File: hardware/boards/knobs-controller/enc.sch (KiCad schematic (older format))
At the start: 11 parts, among them SW2 Rotary Encoder

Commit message: minor cleanup
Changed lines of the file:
@@
 $Descr A4 11693 8268
 encoding utf-8
-Sheet 5 6
+Sheet 3 6
 Title ""
 Date ""
@@
 AR Path="/5D86641C/5D8716A9/5D98B23E" Ref="SW3"  Part="1"
 AR Path="/5D86641C/5D87B0CB/5D98B23E" Ref="SW?"  Part="1"
-F 0 "SW3" H 5500 4570 70  0000 L BNN
+F 0 "SW2" H 5500 4570 70  0000 L BNN
 F 1 "Rotary Encoder" H 5500 3655 70  0000 L BNN
 F 2 "knobs:ENCODER_LED_3_KIT" H 6000 4150 50  0001 C CNN
@@
 AR Path="/5D86641C/5D8716A9/5D98B244" Ref="R28"  Part="1"
 AR Path="/5D86641C/5D87B0CB/5D98B244" Ref="R?"  Part="1"
-F 0 "R28" H 6850 5059 59  0000 L BNN
+F 0 "R19" H 6850 5059 59  0000 L BNN
 F 1 "10k" H 6850 4870 59  0000 L BNN
 F 2 "knobs:R0805" H 7000 5000 50  0001 C CNN
@@
 AR Path="/5D86641C/5D8716A9/5D98B24A" Ref="R25"  Part="1"
 AR Path="/5D86641C/5D87B0CB/5D98B24A" Ref="R?"  Part="1"
-F 0 "R25" H 4050 3709 59  0000 L BNN
+F 0 "R12" H 4050 3709 59  0000 L BNN
 F 1 "10k" H 4050 3520 59  0000 L BNN
 F 2 "knobs:R0805" H 4200 3650 50  0001 C CNN
@@
 AR Path="/5D86641C/5D8716A9/5D98B250" Ref="R24"  Part="1"
 AR Path="/5D86641C/5D87B0CB/5D98B250" Ref="R?"  Part="1"
-F 0 "R24" H 3750 4009 59  0000 L BNN
+F 0 "R11" H 3750 4009 59  0000 L BNN
 F 1 "10k" H 3750 3820 59  0000 L BNN
 F 2 "knobs:R0805" H 3900 3950 50  0001 C CNN
@@
 AR Path="/5D86641C/5D8716A9/5D98B256" Ref="R27"  Part="1"
 AR Path="/5D86641C/5D87B0CB/5D98B256" Ref="R?"  Part="1"
-F 0 "R27" H 5050 3709 59  0000 L BNN
+F 0 "R17" H 5050 3709 59  0000 L BNN
 F 1 "10k" H 5050 3520 59  0000 L BNN
 F 2 "knobs:R0805" H 5200 3650 50  0001 C CNN
@@
 AR Path="/5D86641C/5D8716A9/5D98B25C" Ref="R26"  Part="1"
 AR Path="/5D86641C/5D87B0CB/5D98B25C" Ref="R?"  Part="1"
-F 0 "R26" H 4750 4409 59  0000 L BNN
+F 0 "R14" H 4750 4409 59  0000 L BNN
 F 1 "10k" H 4750 4220 59  0000 L BNN
 F 2 "knobs:R0805" H 4900 4350 50  0001 C CNN
@@
 AR Path="/5D86641C/5D8716A9/5D98B262" Ref="C14"  Part="1"
 AR Path="/5D86641C/5D87B0CB/5D98B262" Ref="C?"  Part="1"
-F 0 "C14" H 4660 4765 59  0000 L BNN
+F 0 "C12" H 4660 4765 59  0000 L BNN
 F 1 "10nF" H 4660 4465 59  0001 L BNN
 F 2 "knobs:C0805" H 4600 4650 50  0001 C CNN
@@
 AR Path="/5D86641C/5D8716A9/5D98B268" Ref="C13"  Part="1"
 AR Path="/5D86641C/5D87B0CB/5D98B268" Ref="C?"  Part="1"
-F 0 "C13" H 3660 4265 59  0000 L BNN
+F 0 "C3" H 3660 4265 59  0000 L BNN
 F 1 "10nF" H 3660 4065 59  0000 L BNN
 F 2 "knobs:C0805" H 3600 4250 50  0001 C CNN
@@
 AR Path="/5D86641C/5D8716A9/5D98B26E" Ref="R29"  Part="1"
 AR Path="/5D86641C/5D87B0CB/5D98B26E" Ref="R?"  Part="1"
-F 0 "R29" H 7050 3909 59  0000 L BNN
+F 0 "R21" H 7050 3909 59  0000 L BNN
 F 1 "10" H 7050 3720 59  0000 L BNN
 F 2 "knobs:R0805" H 7200 3850 50  0001 C CNN
@@
 AR Path="/5D86641C/5D8716A9/5D98B274" Ref="R30"  Part="1"
 AR Path="/5D86641C/5D87B0CB/5D98B274" Ref="R?"  Part="1"
-F 0 "R30" H 7050 4209 59  0000 L BNN
+F 0 "R22" H 7050 4209 59  0000 L BNN
 F 1 "10" H 7050 4020 59  0000 L BNN
 F 2 "knobs:R0805" H 7200 4150 50  0001 C CNN
@@
 AR Path="/5D86641C/5D8716A9/5D98B27A" Ref="R31"  Part="1"
 AR Path="/5D86641C/5D87B0CB/5D98B27A" Ref="R?"  Part="1"
-F 0 "R31" H 7050 4509 59  0000 L BNN
+F 0 "R23" H 7050 4509 59  0000 L BNN
 F 1 "10" H 7050 4320 59  0000 L BNN
 F 2 "knobs:R0805" H 7200 4450 50  0001 C CNN
@@
 AR Path="/5D86641C/5D8716A9/5D98B281" Ref="#+3V020"  Part="1"
 AR Path="/5D86641C/5D87B0CB/5D98B281" Ref="#+3V?"  Part="1"
-F 0 "#+3V020" H 5200 3250 50  0001 C CNN
+F 0 "#+3V017" H 5200 3250 50  0001 C CNN
 F 1 "+3V3" H 5200 3372 59  0000 C CNN
 F 2 "" H 5200 3250 50  0001 C CNN
@@
 AR Path="/5D86641C/5D8716A9/5D98B287" Ref="#GND030"  Part="1"
 AR Path="/5D86641C/5D87B0CB/5D98B287" Ref="#GND?"  Part="1"
-F 0 "#GND030" H 4600 4950 50  0001 C CNN
+F 0 "#GND026" H 4600 4950 50  0001 C CNN
 F 1 "GND" H 4600 4829 59  0000 C CNN
 F 2 "" H 4600 4950 50  0001 C CNN
@@
 AR Path="/5D86641C/5D8716A9/5D98B28D" Ref="#+3V019"  Part="1"
 AR Path="/5D86641C/5D87B0CB/5D98B28D" Ref="#+3V?"  Part="1"
-F 0 "#+3V019" H 4200 3250 50  0001 C CNN
+F 0 "#+3V016" H 4200 3250 50  0001 C CNN
 F 1 "+3V3" H 4200 3372 59  0000 C CNN
 F 2 "" H 4200 3250 50  0001 C CNN
@@
 AR Path="/5D86641C/5D8716A9/5D98B293" Ref="#+3V021"  Part="1"
 AR Path="/5D86641C/5D87B0CB/5D98B293" Ref="#+3V?"  Part="1"
-F 0 "#+3V021" H 6700 3650 50  0001 C CNN
+F 0 "#+3V018" H 6700 3650 50  0001 C CNN
 F 1 "+3V3" H 6700 3772 59  0000 C CNN
 F 2 "" H 6700 3650 50  0001 C CNN
@@
 AR Path="/5D86641C/5D8716A9/5D98B299" Ref="#GND029"  Part="1"
 AR Path="/5D86641C/5D87B0CB/5D98B299" Ref="#GND?"  Part="1"
-F 0 "#GND029" H 3600 4550 50  0001 C CNN
+F 0 "#GND025" H 3600 4550 50  0001 C CNN
 F 1 "GND" H 3600 4429 59  0000 C CNN
 F 2 "" H 3600 4550 50  0001 C CNN
@@
 AR Path="/5D86641C/5D8716A9/5D98B29F" Ref="#GND032"  Part="1"
 AR Path="/5D86641C/5D87B0CB/5D98B29F" Ref="#GND?"  Part="1"
-F 0 "#GND032" H 7000 5300 50  0001 C CNN
+F 0 "#GND028" H 7000 5300 50  0001 C CNN
 F 1 "GND" H 7000 5179 59  0000 C CNN
 F 2 "" H 7000 5300 50  0001 C CNN
@@
 AR Path="/5D86641C/5D8716A9/5D98B2A5" Ref="#GND031"  Part="1"
 AR Path="/5D86641C/5D87B0CB/5D98B2A5" Ref="#GND?"  Part="1"
-F 0 "#GND031" H 5300 4550 50  0001 C CNN
+F 0 "#GND027" H 5300 4550 50  0001 C CNN
 F 1 "GND" H 5300 4429 59  0000 C CNN
 F 2 "" H 5300 4550 50  0001 C CNN

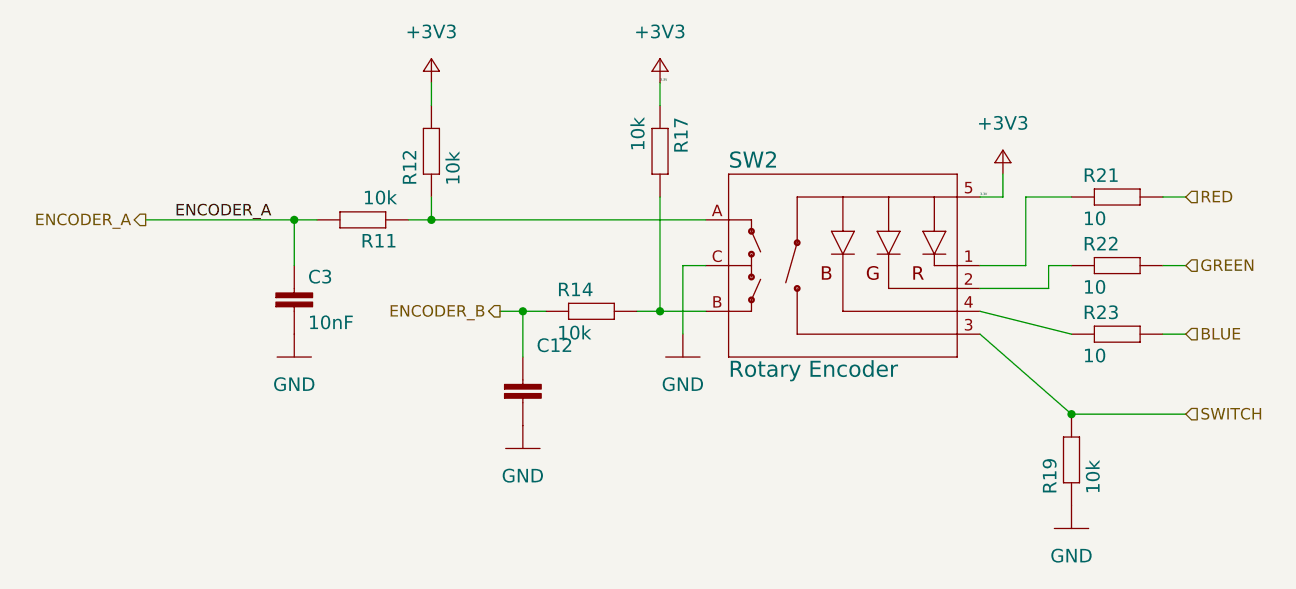
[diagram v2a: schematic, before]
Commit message: correction: tx, rx connected
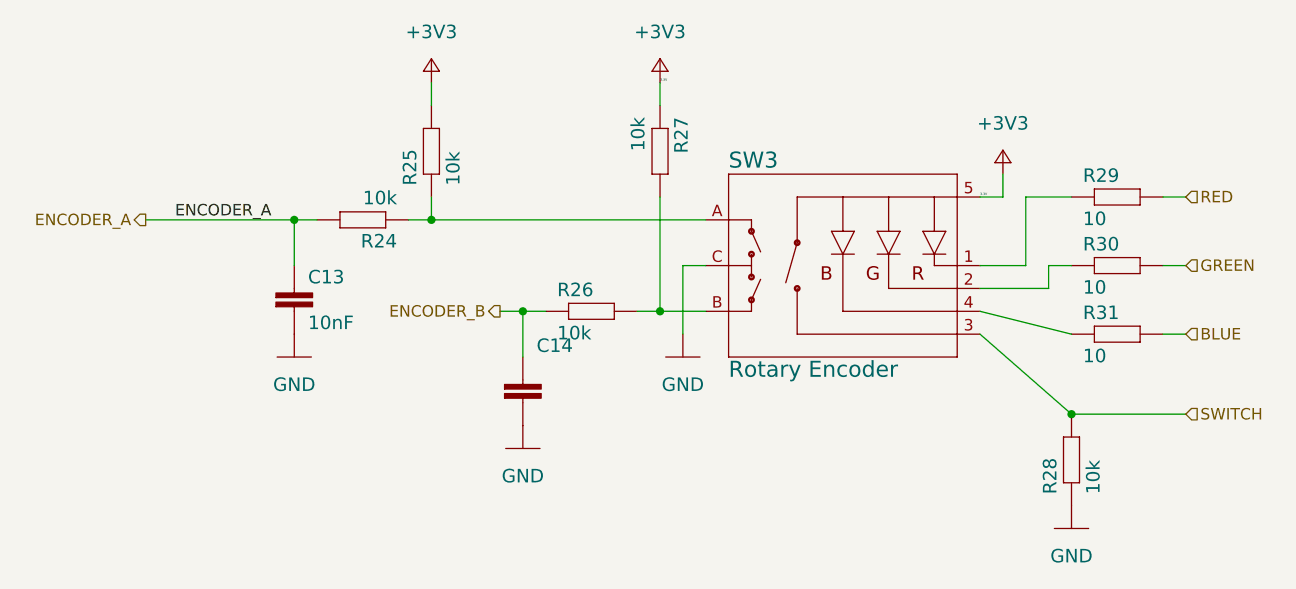
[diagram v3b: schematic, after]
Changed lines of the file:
@@
-EESchema Schematic File Version 4
-LIBS:knobs-cache
+EESchema Schematic File Version 5
 EELAYER 30 0
 EELAYER END
@@
 Comment3 ""
 Comment4 ""
+Comment5 ""
+Comment6 ""
+Comment7 ""
+Comment8 ""
+Comment9 ""
 $EndDescr
 Wire Wire Line
@@
 AR Path="/5D86641C/5D8716A9/5D98B23E" Ref="SW3"  Part="1"
 AR Path="/5D86641C/5D87B0CB/5D98B23E" Ref="SW?"  Part="1"
-F 0 "SW2" H 5500 4570 70  0000 L BNN
+F 0 "SW3" H 5500 4570 70  0000 L BNN
 F 1 "Rotary Encoder" H 5500 3655 70  0000 L BNN
 F 2 "knobs:ENCODER_LED_3_KIT" H 6000 4150 50  0001 C CNN
@@
 AR Path="/5D86641C/5D8716A9/5D98B244" Ref="R28"  Part="1"
 AR Path="/5D86641C/5D87B0CB/5D98B244" Ref="R?"  Part="1"
-F 0 "R19" H 6850 5059 59  0000 L BNN
+F 0 "R28" H 6850 5059 59  0000 L BNN
 F 1 "10k" H 6850 4870 59  0000 L BNN
 F 2 "knobs:R0805" H 7000 5000 50  0001 C CNN
@@
 AR Path="/5D86641C/5D8716A9/5D98B24A" Ref="R25"  Part="1"
 AR Path="/5D86641C/5D87B0CB/5D98B24A" Ref="R?"  Part="1"
-F 0 "R12" H 4050 3709 59  0000 L BNN
+F 0 "R25" H 4050 3709 59  0000 L BNN
 F 1 "10k" H 4050 3520 59  0000 L BNN
 F 2 "knobs:R0805" H 4200 3650 50  0001 C CNN
@@
 AR Path="/5D86641C/5D8716A9/5D98B250" Ref="R24"  Part="1"
 AR Path="/5D86641C/5D87B0CB/5D98B250" Ref="R?"  Part="1"
-F 0 "R11" H 3750 4009 59  0000 L BNN
+F 0 "R24" H 3750 4009 59  0000 L BNN
 F 1 "10k" H 3750 3820 59  0000 L BNN
 F 2 "knobs:R0805" H 3900 3950 50  0001 C CNN
@@
 AR Path="/5D86641C/5D8716A9/5D98B256" Ref="R27"  Part="1"
 AR Path="/5D86641C/5D87B0CB/5D98B256" Ref="R?"  Part="1"
-F 0 "R17" H 5050 3709 59  0000 L BNN
+F 0 "R27" H 5050 3709 59  0000 L BNN
 F 1 "10k" H 5050 3520 59  0000 L BNN
 F 2 "knobs:R0805" H 5200 3650 50  0001 C CNN
@@
 AR Path="/5D86641C/5D8716A9/5D98B25C" Ref="R26"  Part="1"
 AR Path="/5D86641C/5D87B0CB/5D98B25C" Ref="R?"  Part="1"
-F 0 "R14" H 4750 4409 59  0000 L BNN
+F 0 "R26" H 4750 4409 59  0000 L BNN
 F 1 "10k" H 4750 4220 59  0000 L BNN
 F 2 "knobs:R0805" H 4900 4350 50  0001 C CNN
@@
 AR Path="/5D86641C/5D8716A9/5D98B262" Ref="C14"  Part="1"
 AR Path="/5D86641C/5D87B0CB/5D98B262" Ref="C?"  Part="1"
-F 0 "C12" H 4660 4765 59  0000 L BNN
+F 0 "C14" H 4660 4765 59  0000 L BNN
 F 1 "10nF" H 4660 4465 59  0001 L BNN
 F 2 "knobs:C0805" H 4600 4650 50  0001 C CNN
@@
 AR Path="/5D86641C/5D8716A9/5D98B268" Ref="C13"  Part="1"
 AR Path="/5D86641C/5D87B0CB/5D98B268" Ref="C?"  Part="1"
-F 0 "C3" H 3660 4265 59  0000 L BNN
+F 0 "C13" H 3660 4265 59  0000 L BNN
 F 1 "10nF" H 3660 4065 59  0000 L BNN
 F 2 "knobs:C0805" H 3600 4250 50  0001 C CNN
@@
 AR Path="/5D86641C/5D8716A9/5D98B26E" Ref="R29"  Part="1"
 AR Path="/5D86641C/5D87B0CB/5D98B26E" Ref="R?"  Part="1"
-F 0 "R21" H 7050 3909 59  0000 L BNN
+F 0 "R29" H 7050 3909 59  0000 L BNN
 F 1 "10" H 7050 3720 59  0000 L BNN
 F 2 "knobs:R0805" H 7200 3850 50  0001 C CNN
@@
 AR Path="/5D86641C/5D8716A9/5D98B274" Ref="R30"  Part="1"
 AR Path="/5D86641C/5D87B0CB/5D98B274" Ref="R?"  Part="1"
-F 0 "R22" H 7050 4209 59  0000 L BNN
+F 0 "R30" H 7050 4209 59  0000 L BNN
 F 1 "10" H 7050 4020 59  0000 L BNN
 F 2 "knobs:R0805" H 7200 4150 50  0001 C CNN
@@
 AR Path="/5D86641C/5D8716A9/5D98B27A" Ref="R31"  Part="1"
 AR Path="/5D86641C/5D87B0CB/5D98B27A" Ref="R?"  Part="1"
-F 0 "R23" H 7050 4509 59  0000 L BNN
+F 0 "R31" H 7050 4509 59  0000 L BNN
 F 1 "10" H 7050 4320 59  0000 L BNN
 F 2 "knobs:R0805" H 7200 4450 50  0001 C CNN

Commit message: v1.7: merge knobs and top breakout in to single board, remove fpc connector, replace with standard 0.1' pin header
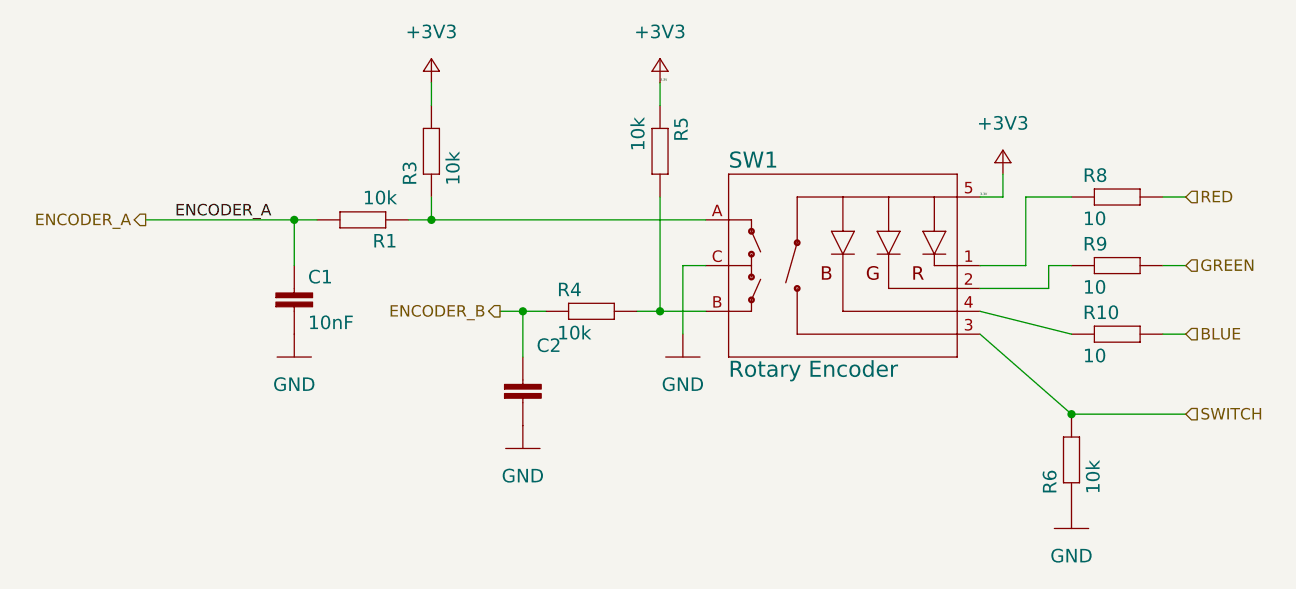
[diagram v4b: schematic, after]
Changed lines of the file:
@@
-EESchema Schematic File Version 5
+EESchema Schematic File Version 4
 EELAYER 30 0
 EELAYER END
 $Descr A4 11693 8268
 encoding utf-8
-Sheet 3 6
+Sheet 4 13
 Title ""
 Date ""
@@
 Comment3 ""
 Comment4 ""
-Comment5 ""
-Comment6 ""
-Comment7 ""
-Comment8 ""
-Comment9 ""
 $EndDescr
 Wire Wire Line
@@
 AR Path="/5D86641C/5D8716A9/5D98B23E" Ref="SW3"  Part="1"
 AR Path="/5D86641C/5D87B0CB/5D98B23E" Ref="SW?"  Part="1"
-F 0 "SW3" H 5500 4570 70  0000 L BNN
+F 0 "SW1" H 5500 4570 70  0000 L BNN
 F 1 "Rotary Encoder" H 5500 3655 70  0000 L BNN
 F 2 "knobs:ENCODER_LED_3_KIT" H 6000 4150 50  0001 C CNN
@@
 AR Path="/5D86641C/5D8716A9/5D98B244" Ref="R28"  Part="1"
 AR Path="/5D86641C/5D87B0CB/5D98B244" Ref="R?"  Part="1"
-F 0 "R28" H 6850 5059 59  0000 L BNN
+F 0 "R6" H 6850 5059 59  0000 L BNN
 F 1 "10k" H 6850 4870 59  0000 L BNN
 F 2 "knobs:R0805" H 7000 5000 50  0001 C CNN
@@
 AR Path="/5D86641C/5D8716A9/5D98B24A" Ref="R25"  Part="1"
 AR Path="/5D86641C/5D87B0CB/5D98B24A" Ref="R?"  Part="1"
-F 0 "R25" H 4050 3709 59  0000 L BNN
+F 0 "R3" H 4050 3709 59  0000 L BNN
 F 1 "10k" H 4050 3520 59  0000 L BNN
 F 2 "knobs:R0805" H 4200 3650 50  0001 C CNN
@@
 AR Path="/5D86641C/5D8716A9/5D98B250" Ref="R24"  Part="1"
 AR Path="/5D86641C/5D87B0CB/5D98B250" Ref="R?"  Part="1"
-F 0 "R24" H 3750 4009 59  0000 L BNN
+F 0 "R1" H 3750 4009 59  0000 L BNN
 F 1 "10k" H 3750 3820 59  0000 L BNN
 F 2 "knobs:R0805" H 3900 3950 50  0001 C CNN
@@
 AR Path="/5D86641C/5D8716A9/5D98B256" Ref="R27"  Part="1"
 AR Path="/5D86641C/5D87B0CB/5D98B256" Ref="R?"  Part="1"
-F 0 "R27" H 5050 3709 59  0000 L BNN
+F 0 "R5" H 5050 3709 59  0000 L BNN
 F 1 "10k" H 5050 3520 59  0000 L BNN
 F 2 "knobs:R0805" H 5200 3650 50  0001 C CNN
@@
 AR Path="/5D86641C/5D8716A9/5D98B25C" Ref="R26"  Part="1"
 AR Path="/5D86641C/5D87B0CB/5D98B25C" Ref="R?"  Part="1"
-F 0 "R26" H 4750 4409 59  0000 L BNN
+F 0 "R4" H 4750 4409 59  0000 L BNN
 F 1 "10k" H 4750 4220 59  0000 L BNN
 F 2 "knobs:R0805" H 4900 4350 50  0001 C CNN
@@
 AR Path="/5D86641C/5D8716A9/5D98B262" Ref="C14"  Part="1"
 AR Path="/5D86641C/5D87B0CB/5D98B262" Ref="C?"  Part="1"
-F 0 "C14" H 4660 4765 59  0000 L BNN
+F 0 "C2" H 4660 4765 59  0000 L BNN
 F 1 "10nF" H 4660 4465 59  0001 L BNN
 F 2 "knobs:C0805" H 4600 4650 50  0001 C CNN
@@
 AR Path="/5D86641C/5D8716A9/5D98B268" Ref="C13"  Part="1"
 AR Path="/5D86641C/5D87B0CB/5D98B268" Ref="C?"  Part="1"
-F 0 "C13" H 3660 4265 59  0000 L BNN
+F 0 "C1" H 3660 4265 59  0000 L BNN
 F 1 "10nF" H 3660 4065 59  0000 L BNN
 F 2 "knobs:C0805" H 3600 4250 50  0001 C CNN
@@
 AR Path="/5D86641C/5D8716A9/5D98B26E" Ref="R29"  Part="1"
 AR Path="/5D86641C/5D87B0CB/5D98B26E" Ref="R?"  Part="1"
-F 0 "R29" H 7050 3909 59  0000 L BNN
+F 0 "R8" H 7050 3909 59  0000 L BNN
 F 1 "10" H 7050 3720 59  0000 L BNN
 F 2 "knobs:R0805" H 7200 3850 50  0001 C CNN
@@
 AR Path="/5D86641C/5D8716A9/5D98B274" Ref="R30"  Part="1"
 AR Path="/5D86641C/5D87B0CB/5D98B274" Ref="R?"  Part="1"
-F 0 "R30" H 7050 4209 59  0000 L BNN
+F 0 "R9" H 7050 4209 59  0000 L BNN
 F 1 "10" H 7050 4020 59  0000 L BNN
 F 2 "knobs:R0805" H 7200 4150 50  0001 C CNN
@@
 AR Path="/5D86641C/5D8716A9/5D98B27A" Ref="R31"  Part="1"
 AR Path="/5D86641C/5D87B0CB/5D98B27A" Ref="R?"  Part="1"
-F 0 "R31" H 7050 4509 59  0000 L BNN
+F 0 "R10" H 7050 4509 59  0000 L BNN
 F 1 "10" H 7050 4320 59  0000 L BNN
 F 2 "knobs:R0805" H 7200 4450 50  0001 C CNN

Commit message: mainboard v1.7
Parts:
- renumbered C3 to C7, C12 to C8, R14 to R10, R17 to R11, R19 to R12, R21 to R13, R22 to R14, R23 to R15, R11 to R8, R12 to R9, SW2 to SW1
